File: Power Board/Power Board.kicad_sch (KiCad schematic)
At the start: 202 parts, among them IC1 LTC4151IMS#PBF, IC2 LTC4151IMS#PBF, J1 Conn_01x02, J10 Conn_01x02, J11 Conn_01x02, J12 Conn_01x02, J13 Conn_01x02, J14 Conn_01x02, J15 Conn_01x02, J16 Conn_01x02, J17 Conn_01x02, J18 Conn_02x03_Top_Bottom, J2 Conn_01x02, J20 Conn_02x03_Top_Bottom, J3 Conn_01x02, J4 Conn_01x02, J5 Conn_01x02, J6 Conn_01x02, J7 Conn_01x02, J8 Conn_01x02, J9 Conn_02x03_Top_Bottom, Q1 Q_PMOS_GDS, Q10 Q_NMOS_GDS, Q11 Q_NMOS_GDS, Q12 Q_NMOS_GDS, Q13 Q_NMOS_GDS, Q14 Q_NMOS_GDS, Q15 Q_NMOS_GDS, Q16 Q_NMOS_GDS, Q17 Q_NMOS_GDS, Q18 Q_NMOS_GDS, Q19 Q_NMOS_GDS, Q2 Q_PMOS_GDS, Q20 Q_NMOS_GDS, Q21 Q_NMOS_GDS, Q22 Q_NMOS_GDS, Q3 Q_PMOS_GDS, Q4 Q_PMOS_GDS, Q5 Q_PMOS_GDS, Q6 Q_PMOS_GDS, Q7 Q_PMOS_GDS, Q8 Q_PMOS_GDS, Q9 Q_NMOS_GDS, U1 LTC4372CDD-PBF, U10 ACS770xCB-050U-PFF, U11 ACS770xCB-050U-PFF, U12 ACS770xCB-050U-PFF, U13 ACS770xCB-050U-PFF, U14 ACS770xCB-050U-PFF, U15 ADC128S052CIMT, U16 ADC128S052CIMT, U17 TLV70033_SOT23-5, U2 LTC4372CDD-PBF, U3 LTC4372CDD-PBF, U4 LTC4372CDD-PBF, U5 LTC4372CDD-PBF, U6 LTC4372CDD-PBF, U7 LTC4372CDD-PBF, U8 ACS770xCB-050U-PFF, U9 ACS770xCB-050U-PFF

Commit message: i2c routing
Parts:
- added PS3: TEN_50-2411WI, TEN502411WI, symbol TEN_50-2411WI:TEN_50-2411WI
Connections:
- net GNDD: now also J_I2C1.2 (Pin_2); no longer J_I2C1.4 (Pin_4)
- net SCL: now also J_I2C1.4 (Pin_4); no longer J_I2C1.2 (Pin_2)
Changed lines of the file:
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@@
 		)
 	)
-	(label "SCL"
-		(at 54.61 260.35 180)
-		(effects
-			(font
-				(size 1.27 1.27)
-			)
-			(justify right bottom)
-		)
-	)
 	(label "THERM_7"
 		(at 444.5 179.07 0)
@@
 		)
 	)
+	(label "SCL"
+		(at 67.31 257.81 0)
+		(effects
+			(font
+				(size 1.27 1.27)
+			)
+			(justify left bottom)
+		)
+	)
 	(label "24V_UNREGULATED"
 		(at 292.1 179.07 180)
@@
 	(symbol
 		(lib_id "power:GNDD")
-		(at 67.31 257.81 90)
+		(at 67.31 260.35 90)
 		(unit 1)
 		(exclude_from_sim no)
@@
 		(fields_autoplaced yes)
 		(property "Reference" "#PWR0106"
-			(at 73.66 257.81 0)
+			(at 73.66 260.35 0)
 			(effects
 				(font
@@
 		)
 		(property "Value" "GNDD"
-			(at 71.12 257.8099 90)
+			(at 71.12 260.3499 90)
 			(effects
 				(font
@@
 		)
 		(property "Footprint" ""
-			(at 67.31 257.81 0)
+			(at 67.31 260.35 0)
 			(effects
 				(font
@@
 		)
 		(property "Datasheet" ""
-			(at 67.31 257.81 0)
+			(at 67.31 260.35 0)
 			(effects
 				(font
@@
 		)
 		(property "Description" "Power symbol creates a global label with name \"GNDD\" , digital ground"
-			(at 67.31 257.81 0)
+			(at 67.31 260.35 0)
 			(effects
 				(font
@@
 		)
 		(instances
-			(project ""
+			(project "Power Board"
 				(path "/52f7cba9-f573-43e9-b6c5-44859a4c1733"
 					(reference "#PWR0106")
@@
 	)
 	(symbol
+		(lib_id "TEN_50-2411WI:TEN_50-2411WI")
+		(at 90.17 262.89 0)
+		(unit 1)
+		(exclude_from_sim no)
+		(in_bom yes)
+		(on_board yes)
+		(dnp no)
+		(fields_autoplaced yes)
+		(property "Reference" "PS3"
+			(at 111.76 255.27 0)
+			(effects
+				(font
+					(size 1.27 1.27)
+				)
+			)
+		)
+		(property "Value" "TEN_50-2411WI"
+			(at 111.76 257.81 0)
+			(effects
+				(font
+					(size 1.27 1.27)
+				)
+			)
+		)
+		(property "Footprint" "TEN502411WI"
+			(at 129.54 357.81 0)
+			(effects
+				(font
+					(size 1.27 1.27)
+				)
+				(justify left top)
+				(hide yes)
+			)
+		)
+		(property "Datasheet" "https://tracopower.com/ten50wi-datasheet/"
+			(at 129.54 457.81 0)
+			(effects
+				(font
+					(size 1.27 1.27)
+				)
+				(justify left top)
+				(hide yes)
+			)
+		)
+		(property "Description" "50 Watt DC/DC converter, industrial, 4:1 input, encapsulated, 2\" x 1\" metal package"
+			(at 90.17 262.89 0)
+			(effects
+				(font
+					(size 1.27 1.27)
+				)
+				(hide yes)
+			)
+		)
+		(property "Height" "11.25"
+			(at 129.54 657.81 0)
+			(effects
+				(font
+					(size 1.27 1.27)
+				)
+				(justify left top)
+				(hide yes)
+			)
+		)
+		(property "Mouser Part Number" "495-TEN50-2411WI"
+			(at 129.54 757.81 0)
+			(effects
+				(font
+					(size 1.27 1.27)
+				)
+				(justify left top)
+				(hide yes)
+			)
+		)
+		(property "Mouser Price/Stock" "https://www.mouser.co.uk/ProductDetail/TRACO-Power/TEN-50-2411WI?qs=ckJk83FOD0X9tzvZCD0OJQ%3D%3D"
+			(at 129.54 857.81 0)
+			(effects
+				(font
+					(size 1.27 1.27)
+				)
+				(justify left top)
+				(hide yes)
+			)
+		)
+		(property "Manufacturer_Name" "Traco Power"
+			(at 129.54 957.81 0)
+			(effects
+				(font
+					(size 1.27 1.27)
+				)
+				(justify left top)
+				(hide yes)
+			)
+		)
+		(property "Manufacturer_Part_Number" "TEN 50-2411WI"
+			(at 129.54 1057.81 0)
+			(effects
+				(font
+					(size 1.27 1.27)
+				)
+				(justify left top)
+				(hide yes)
+			)
+		)
+		(pin "1"
+		)
+		(pin "6"
+		)
+		(pin "2"
+		)
+		(pin "3"
+		)
+		(pin "5"
+		)
+		(pin "4"
+		)
+		(instances
+			(project ""
+				(path "/52f7cba9-f573-43e9-b6c5-44859a4c1733"
+					(reference "PS3")
+					(unit 1)
+				)
+			)
+		)
+	)
+	(symbol
 		(lib_id "Transistor_FET:Q_PMOS_GDS")
 		(at 107.95 100.33 90)
@@
 	(symbol
 		(lib_id "power:GNDD")
-		(at 67.31 260.35 90)
+		(at 54.61 260.35 0)
 		(unit 1)
 		(exclude_from_sim no)
@@
 		(on_board yes)
 		(dnp no)
-		(fields_autoplaced yes)
 		(property "Reference" "#PWR0105"
-			(at 73.66 260.35 0)
+			(at 54.61 266.7 0)
 			(effects
 				(font
@@
 		)
 		(property "Value" "GNDD"
-			(at 71.12 260.3499 90)
+			(at 48.514 260.604 0)
 			(effects
 				(font
 					(size 1.27 1.27)
 				)
-				(justify right)
+				(justify left)
 			)
 		)
 		(property "Footprint" ""
-			(at 67.31 260.35 0)
+			(at 54.61 260.35 0)
 			(effects
 				(font
@@
 		)
 		(property "Datasheet" ""
-			(at 67.31 260.35 0)
+			(at 54.61 260.35 0)
 			(effects
 				(font
@@
 		)
 		(property "Description" "Power symbol creates a global label with name \"GNDD\" , digital ground"
-			(at 67.31 260.35 0)
+			(at 54.61 260.35 0)
 			(effects
 				(font
@@
 		)
 		(instances
-			(project ""
+			(project "Power Board"
 				(path "/52f7cba9-f573-43e9-b6c5-44859a4c1733"
 					(reference "#PWR0105")

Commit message: added M3 mounting holes, removed buck converter (to be replaced with half-brick), added more pours
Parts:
- removed PS3: TEN_50-2411WI, TEN502411WI, symbol TEN_50-2411WI:TEN_50-2411WI
- added C54: 10uF, Capacitor_SMD:C_0805_2012Metric_Pad1.18x1.45mm_HandSolder, symbol Device:C
- added J19, J21: Conn_01x02, symbol Connector_Generic:Conn_01x02
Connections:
- net 24V_UNREGULATED: now also J19.1 (Pin_1); no longer PS2.1 (+VIN)
- net 5V_PSO: now also C54.1, J21.2 (Pin_2); no longer PS2.6 (-VOUT)
- net GND: now also J7.2 (Pin_2), C54.2, J19.2 (Pin_2), J21.1 (Pin_1); no longer J7.1 (Pin_1), PS2.2 (-VIN), PS2.4 (+VOUT)
- net at F7.1: now also J7.1 (Pin_1); no longer J7.2 (Pin_2)
- no-connect marks 10 -> 8
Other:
- moved on the sheet: C52, D9, J7, PS2

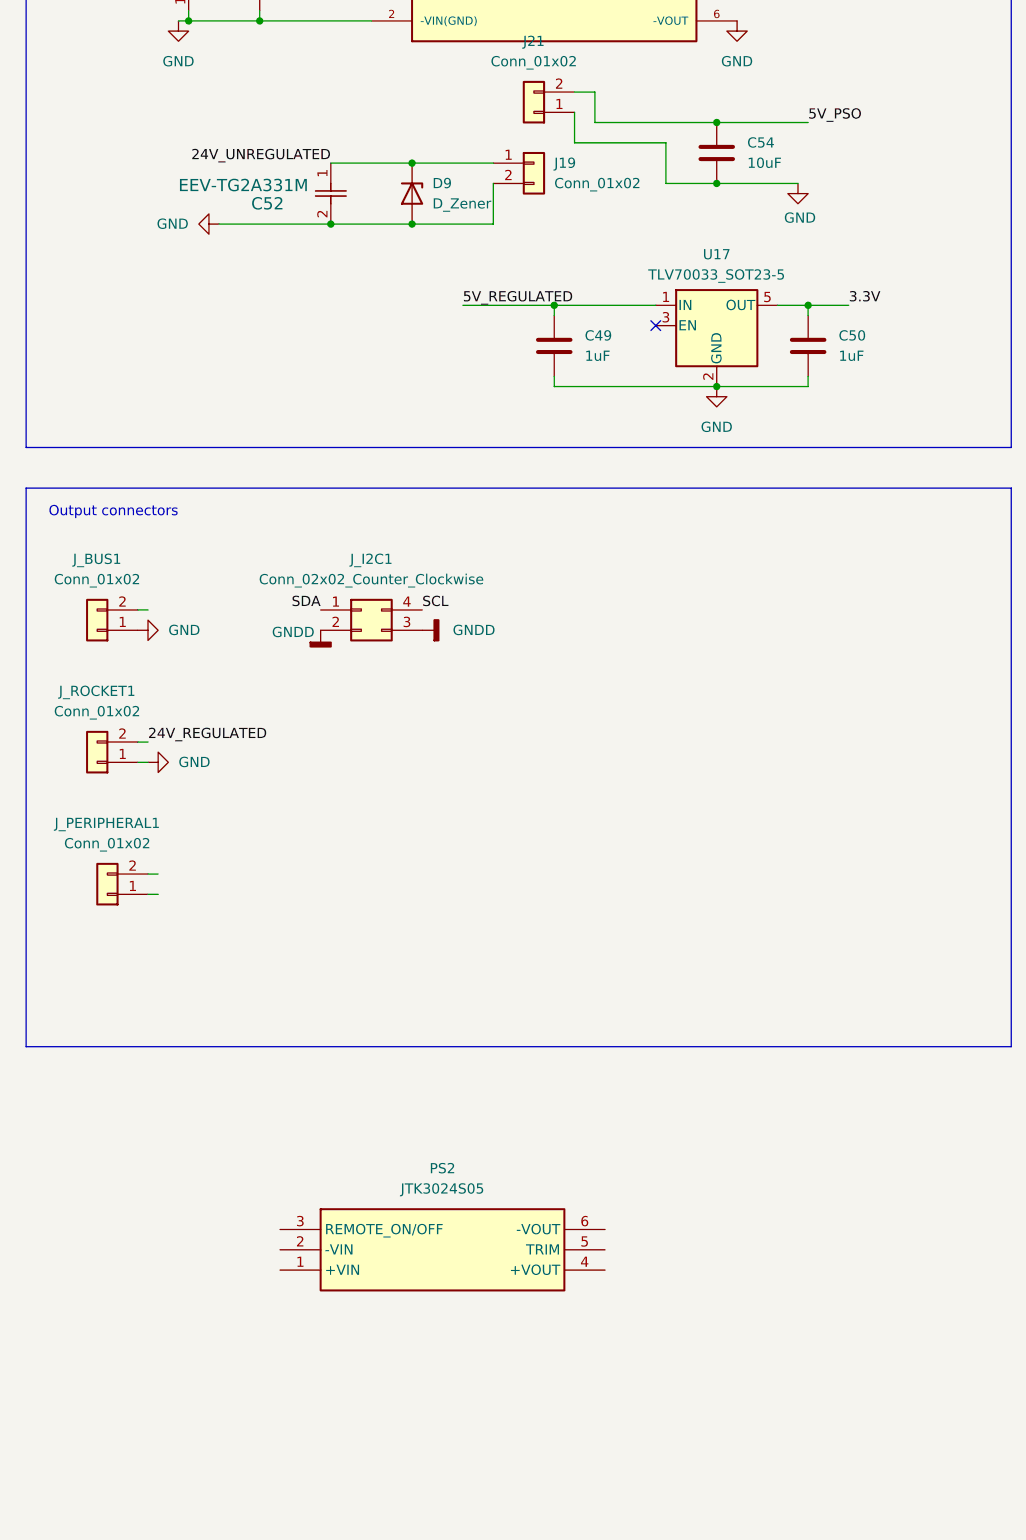
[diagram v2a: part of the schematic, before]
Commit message: added XT60 connectors for 5V rail and standoffs for BMS, 5V converter
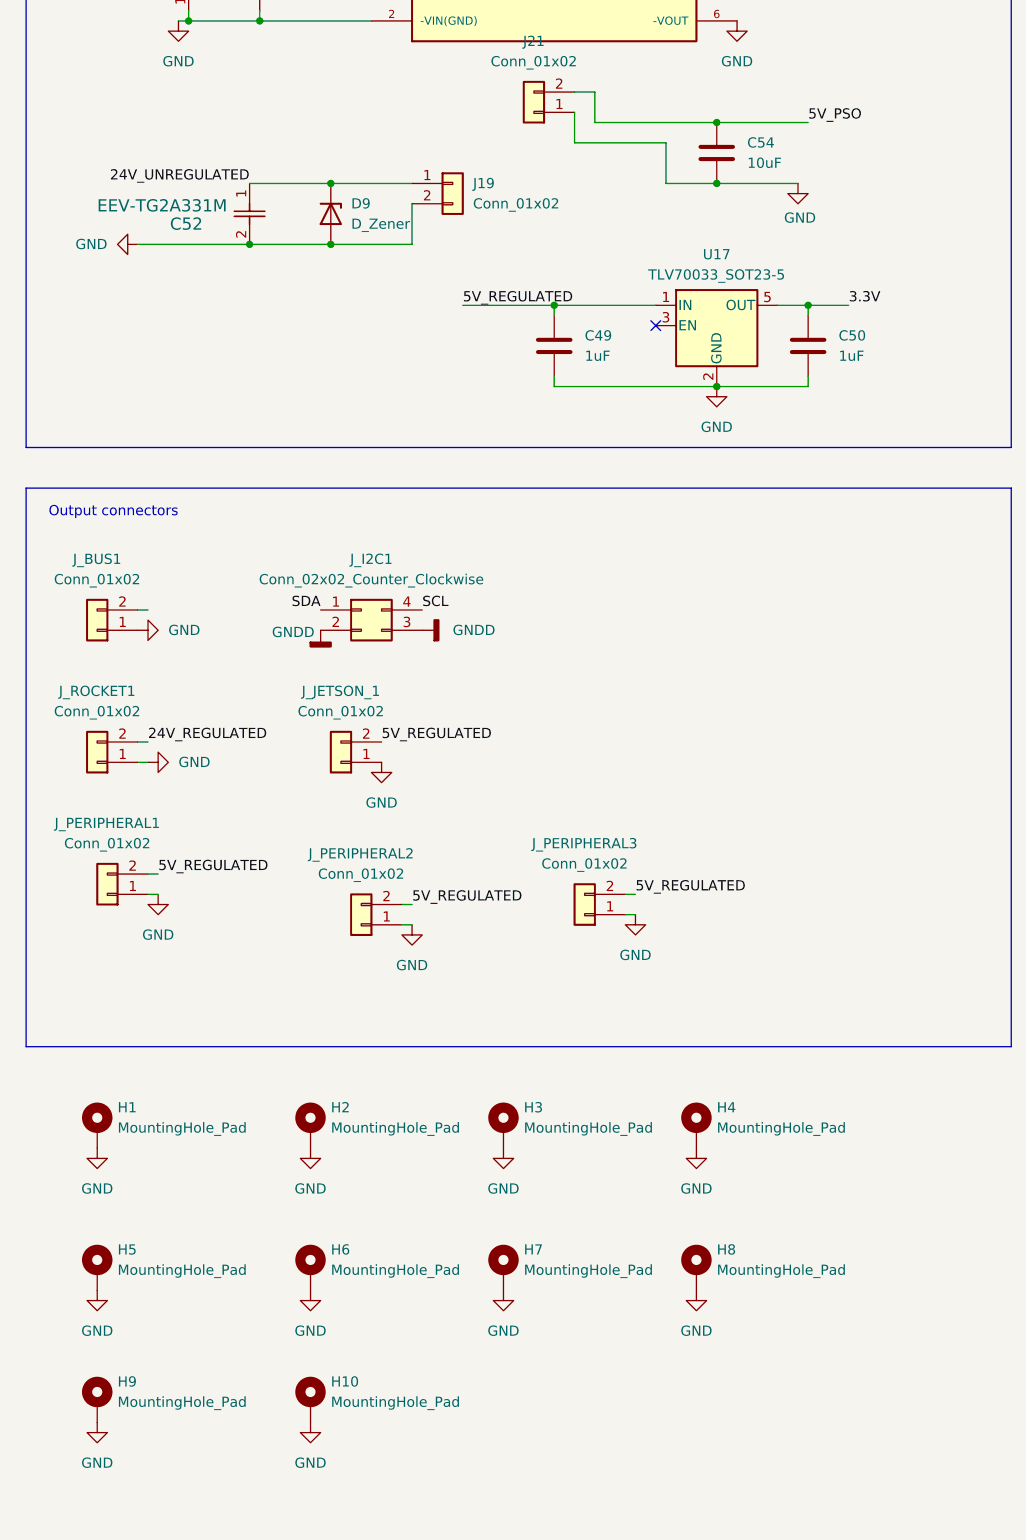
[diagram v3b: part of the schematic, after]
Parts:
- removed PS2: JTK3024S05, JTK3024S05:JTK3024S05, symbol JTK3024S05:JTK3024S05
- added H1, H10, H2, H3, H4, H5, H6, H7, H8, H9: MountingHole_Pad, symbol Mechanical:MountingHole_Pad
- added J_JETSON_1, J_PERIPHERAL2, J_PERIPHERAL3: Conn_01x02, Connector_AMASS:AMASS_XT60-F_1x02_P7.20mm_Vertical, symbol Connector_Generic:Conn_01x02
- J_PERIPHERAL1: footprint (none) -> Connector_AMASS:AMASS_XT60-F_1x02_P7.20mm_Vertical
- J_ROCKET1: footprint Connector_AMASS:AMASS_XT30UPB-F_1x02_P5.0mm_Vertical -> Connector_AMASS:AMASS_XT60-F_1x02_P7.20mm_Vertical
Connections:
- net 5V_REGULATED: now also J_PERIPHERAL1.2 (Pin_2), J_JETSON_1.2 (Pin_2), J_PERIPHERAL2.2 (Pin_2), J_PERIPHERAL3.2 (Pin_2)
- net GND: now also J_PERIPHERAL1.1 (Pin_1), H1.1, H10.1, H2.1, H3.1, H4.1, H5.1, H6.1, H7.1, H8.1, H9.1, J_JETSON_1.1 (Pin_1), J_PERIPHERAL2.1 (Pin_1), J_PERIPHERAL3.1 (Pin_1)
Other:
- moved on the sheet: C52, D9, J19

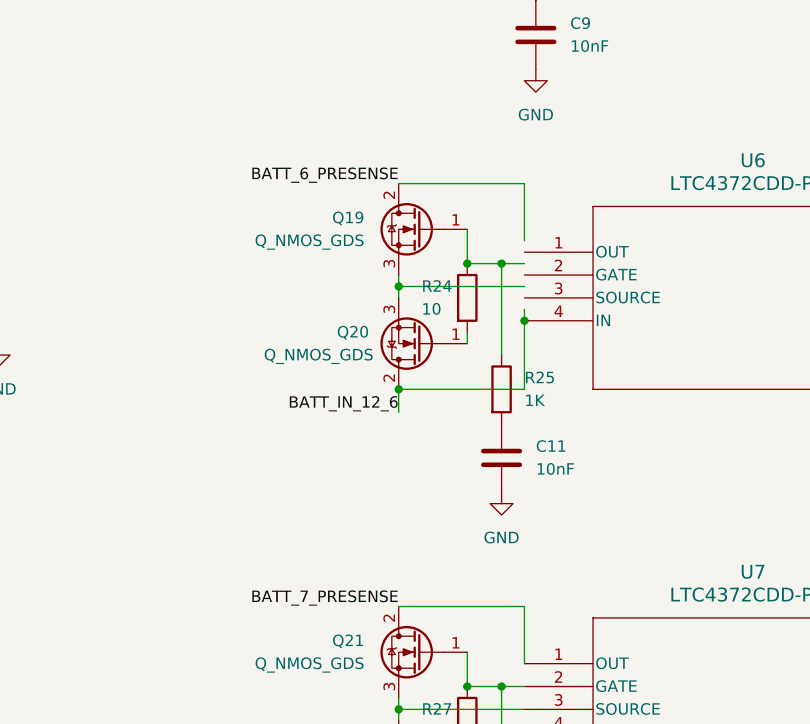
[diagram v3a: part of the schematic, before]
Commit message: minor tracing updates for batteries on PDB
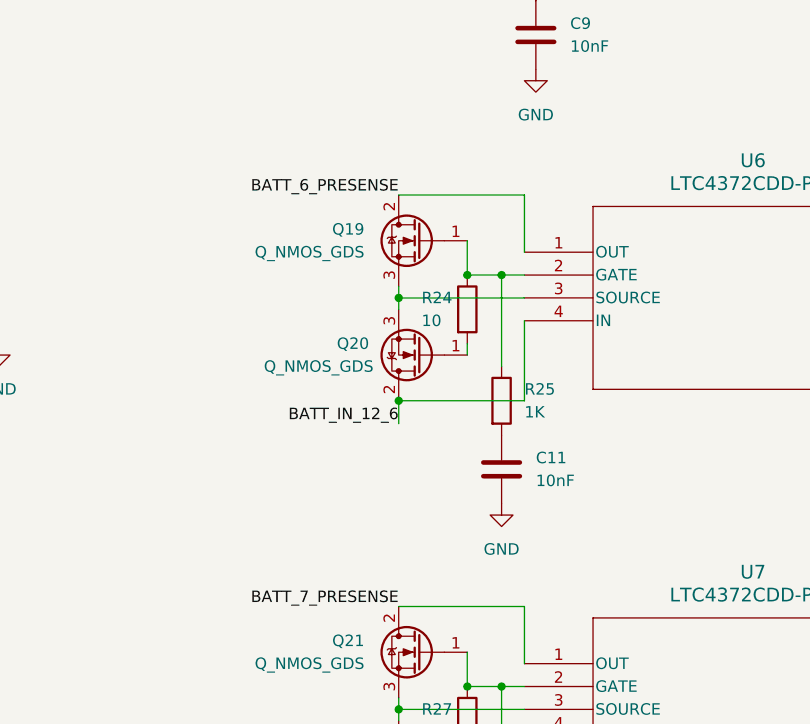
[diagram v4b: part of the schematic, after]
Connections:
- net BATT_6_PRESENSE: now also U6.1 (OUT)
- net at Q19.1 (G), R24.1, R25.1: now also U6.2 (GATE)
- net at Q19.3 (S), Q20.3 (S): now also U6.3 (SOURCE)
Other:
- moved on the sheet: C11, Q19, Q20, R24, R25
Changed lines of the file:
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@@
 	)
 	(junction
-		(at 299.72 83.82)
+		(at 299.72 85.09)
 		(diameter 0)
 		(color 0 0 0 0)
@@
 	)
 	(junction
-		(at 292.1 86.36)
+		(at 292.1 87.63)
 		(diameter 0)
 		(color 0 0 0 0)
@@
 	)
 	(junction
-		(at 292.1 97.79)
+		(at 292.1 99.06)
 		(diameter 0)
 		(color 0 0 0 0)
@@
 	)
 	(junction
-		(at 303.53 83.82)
+		(at 303.53 85.09)
 		(diameter 0)
 		(color 0 0 0 0)
@@
 	)
 	(junction
-		(at 306.07 90.17)
-		(diameter 0)
-		(color 0 0 0 0)
-	)
-	(junction
 		(at 175.26 176.53)
 		(diameter 0)
@@
 	(wire
 		(pts
-			(xy 299.72 83.82) (xy 299.72 80.01)
+			(xy 299.72 85.09) (xy 299.72 81.28)
 		)
 		(stroke
@@
 	(wire
 		(pts
-			(xy 292.1 74.93) (xy 306.07 74.93)
+			(xy 292.1 76.2) (xy 306.07 76.2)
 		)
 		(stroke
@@
 	(wire
 		(pts
-			(xy 306.07 74.93) (xy 306.07 81.28)
+			(xy 306.07 76.2) (xy 306.07 82.55)
 		)
 		(stroke
@@
 	(wire
 		(pts
-			(xy 306.07 86.36) (xy 292.1 86.36)
+			(xy 306.07 87.63) (xy 292.1 87.63)
 		)
 		(stroke
@@
 	(wire
 		(pts
+			(xy 306.07 90.17) (xy 306.07 99.06)
+		)
+		(stroke
+			(width 0)
+			(type default)
+		)
+	)
+	(wire
+		(pts
 			(xy 232.41 88.9) (xy 240.03 88.9)
 		)
@@
 	(wire
 		(pts
-			(xy 292.1 86.36) (xy 292.1 85.09)
+			(xy 292.1 87.63) (xy 292.1 86.36)
 		)
 		(stroke
@@
 	(wire
 		(pts
-			(xy 303.53 83.82) (xy 299.72 83.82)
+			(xy 303.53 85.09) (xy 299.72 85.09)
 		)
 		(stroke
@@
 	(wire
 		(pts
-			(xy 306.07 83.82) (xy 303.53 83.82)
+			(xy 306.07 85.09) (xy 303.53 85.09)
 		)
 		(stroke
@@
 	(wire
 		(pts
-			(xy 306.07 90.17) (xy 306.07 88.9)
-		)
-		(stroke
-			(width 0)
-			(type default)
-		)
-	)
-	(wire
-		(pts
 			(xy 92.71 129.54) (xy 93.98 129.54)
 		)
@@
 	(wire
 		(pts
-			(xy 292.1 86.36) (xy 292.1 87.63)
+			(xy 292.1 87.63) (xy 292.1 88.9)
 		)
 		(stroke
@@
 	(wire
 		(pts
-			(xy 303.53 83.82) (xy 303.53 93.98)
+			(xy 303.53 85.09) (xy 303.53 95.25)
 		)
 		(stroke
@@
 	(wire
 		(pts
-			(xy 306.07 97.79) (xy 306.07 90.17)
-		)
-		(stroke
-			(width 0)
-			(type default)
-		)
-	)
-	(wire
-		(pts
 			(xy 267.97 233.68) (xy 278.13 233.68)
 		)
@@
 	(wire
 		(pts
-			(xy 299.72 91.44) (xy 299.72 92.71)
+			(xy 299.72 92.71) (xy 299.72 93.98)
 		)
 		(stroke
@@
 	(wire
 		(pts
-			(xy 292.1 97.79) (xy 306.07 97.79)
+			(xy 292.1 99.06) (xy 306.07 99.06)
 		)
 		(stroke
@@
 	(wire
 		(pts
-			(xy 292.1 97.79) (xy 292.1 100.33)
+			(xy 292.1 99.06) (xy 292.1 101.6)
 		)
 		(stroke
@@
 	)
 	(label "BATT_6_PRESENSE"
-		(at 292.1 74.93 180)
+		(at 292.1 76.2 180)
 		(effects
 			(font
@@
 	)
 	(label "BATT_IN_12_6"
-		(at 292.1 100.33 180)
+		(at 292.1 101.6 180)
 		(effects
 			(font
@@
 	(symbol
 		(lib_id "Device:R")
-		(at 303.53 97.79 0)
+		(at 303.53 99.06 0)
 		(unit 1)
 		(exclude_from_sim no)
@@
 		(fields_autoplaced yes)
 		(property "Reference" "R25"
-			(at 306.07 96.5199 0)
+			(at 306.07 97.7899 0)
 			(effects
 				(font
@@
 		)
 		(property "Value" "1K"
-			(at 306.07 99.0599 0)
+			(at 306.07 100.3299 0)
 			(effects
 				(font
@@
 		)
 		(property "Footprint" "Resistor_SMD:R_0805_2012Metric_Pad1.20x1.40mm_HandSolder"
-			(at 301.752 97.79 90)
+			(at 301.752 99.06 90)
 			(effects
 				(font
@@
 		)
 		(property "Datasheet" "~"
-			(at 303.53 97.79 0)
+			(at 303.53 99.06 0)
 			(effects
 				(font
@@
 		)
 		(property "Description" ""
-			(at 303.53 97.79 0)
+			(at 303.53 99.06 0)
 			(effects
 				(font
@@
 	(symbol
 		(lib_id "power:GND")
-		(at 303.53 109.22 0)
+		(at 303.53 110.49 0)
 		(unit 1)
 		(exclude_from_sim no)
@@
 		(fields_autoplaced yes)
 		(property "Reference" "#PWR026"
-			(at 303.53 115.57 0)
+			(at 303.53 116.84 0)
 			(effects
 				(font
@@
 		)
 		(property "Value" "GND"
-			(at 303.53 114.3 0)
+			(at 303.53 115.57 0)
 			(effects
 				(font
@@
 		)
 		(property "Footprint" ""
-			(at 303.53 109.22 0)
+			(at 303.53 110.49 0)
 			(effects
 				(font
@@
 		)
 		(property "Datasheet" ""
-			(at 303.53 109.22 0)
+			(at 303.53 110.49 0)
 			(effects
 				(font
@@
 		)
 		(property "Description" ""
-			(at 303.53 109.22 0)
+			(at 303.53 110.49 0)
 			(effects
 				(font
@@
 	(symbol
 		(lib_id "Device:Q_NMOS_GDS")
-		(at 294.64 92.71 180)
+		(at 294.64 93.98 180)
 		(unit 1)
 		(exclude_from_sim no)
@@
 		(dnp no)
 		(property "Reference" "Q20"
-			(at 287.02 91.44 0)
+			(at 287.02 92.71 0)
 			(effects
 				(font
@@
 		)
 		(property "Value" "Q_NMOS_GDS"
-			(at 283.21 93.98 0)
+			(at 283.21 95.25 0)
 			(effects
 				(font
@@
 		)
 		(property "Footprint" "Package_SO:PowerPAK_SO-8_Single"
-			(at 289.56 95.25 0)
+			(at 289.56 96.52 0)
 			(effects
 				(font
@@
 		)
 		(property "Datasheet" "~"
-			(at 294.64 92.71 0)
+			(at 294.64 93.98 0)
 			(effects
 				(font
@@
 		)
 		(property "Description" ""
-			(at 294.64 92.71 0)
+			(at 294.64 93.98 0)
 			(effects
 				(font
@@
 	(symbol
 		(lib_id "Device:R")
-		(at 299.72 87.63 0)
+		(at 299.72 88.9 0)
 		(unit 1)
 		(exclude_from_sim no)
@@
 		(dnp no)
 		(property "Reference" "R24"
-			(at 294.64 86.36 0)
+			(at 294.64 87.63 0)
 			(effects
 				(font
@@
 		)
 		(property "Value" "10"
-			(at 294.64 88.9 0)
+			(at 294.64 90.17 0)
 			(effects
 				(font
@@
 		)
 		(property "Footprint" "Resistor_SMD:R_0805_2012Metric_Pad1.20x1.40mm_HandSolder"
-			(at 297.942 87.63 90)
+			(at 297.942 88.9 90)
 			(effects
 				(font
@@
 		)
 		(property "Datasheet" "~"
-			(at 299.72 87.63 0)
+			(at 299.72 88.9 0)
 			(effects
 				(font
@@
 		)
 		(property "Description" ""
-			(at 299.72 87.63 0)
+			(at 299.72 88.9 0)
 			(effects
 				(font
@@
 	(symbol
 		(lib_id "Device:C")
-		(at 303.53 105.41 0)
+		(at 303.53 106.68 0)
 		(unit 1)
 		(exclude_from_sim no)
@@
 		(fields_autoplaced yes)
 		(property "Reference" "C11"
-			(at 307.34 104.1399 0)
+			(at 307.34 105.4099 0)
 			(effects
 				(font
@@
 		)
 		(property "Value" "10nF"
-			(at 307.34 106.6799 0)
+			(at 307.34 107.9499 0)
 			(effects
 				(font
@@
 		)
 		(property "Footprint" "Capacitor_SMD:C_0201_0603Metric_Pad0.64x0.40mm_HandSolder"
-			(at 304.4952 109.22 0)
+			(at 304.4952 110.49 0)
 			(effects
 				(font
@@
 		)
 		(property "Datasheet" "~"
-			(at 303.53 105.41 0)
+			(at 303.53 106.68 0)
 			(effects
 				(font
@@
 		)
 		(property "Description" ""
-			(at 303.53 105.41 0)
+			(at 303.53 106.68 0)
 			(effects
 				(font
@@
 	(symbol
 		(lib_id "Device:Q_NMOS_GDS")
-		(at 294.64 80.01 0)
+		(at 294.64 81.28 0)
 		(mirror y)
 		(unit 1)
@@
 		(fields_autoplaced yes)
 		(property "Reference" "Q19"
-			(at 288.29 78.7399 0)
+			(at 288.29 80.0099 0)
 			(effects
 				(font
@@
 		)
 		(property "Value" "Q_NMOS_GDS"
-			(at 288.29 81.2799 0)
+			(at 288.29 82.5499 0)
 			(effects
 				(font
@@
 		)
 		(property "Footprint" "Package_SO:PowerPAK_SO-8_Single"
-			(at 289.56 77.47 0)
+			(at 289.56 78.74 0)
 			(effects
 				(font
@@
 		)
 		(property "Datasheet" "~"
-			(at 294.64 80.01 0)
+			(at 294.64 81.28 0)
 			(effects
 				(font
@@
 		)
 		(property "Description" ""
-			(at 294.64 80.01 0)
+			(at 294.64 81.28 0)
 			(effects
 				(font
